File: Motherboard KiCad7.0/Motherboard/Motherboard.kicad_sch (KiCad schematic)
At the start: 49 parts, among them J1 USB_B_Micro, J2 SWD_01x04_Pin, Q1 AO3400A, SW1 SW_STM_RESET, SW2 SW_STM_BOOT_MODE, U1 STM32F103CBT6, U2 AMS1117-3.3, U3 LM66100DCKR, U4 LM66100DCKR, U5 LM66100DCKR, Y1 X322516MMB4SI

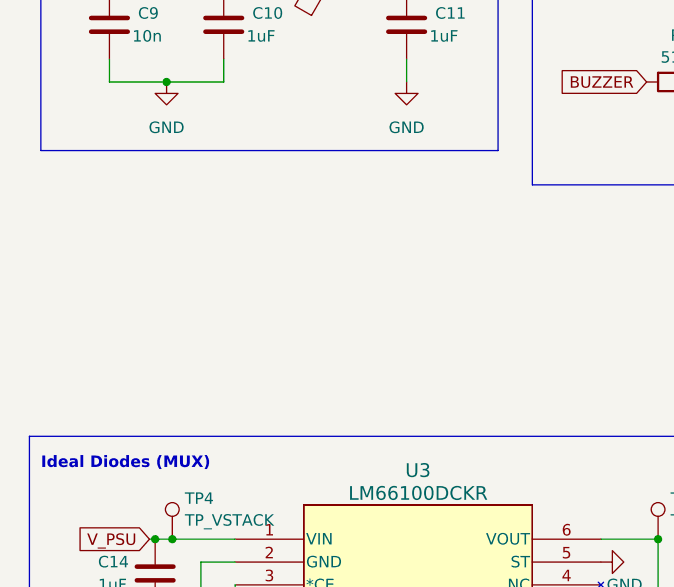
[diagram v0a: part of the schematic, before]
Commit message: Solenoid Valve
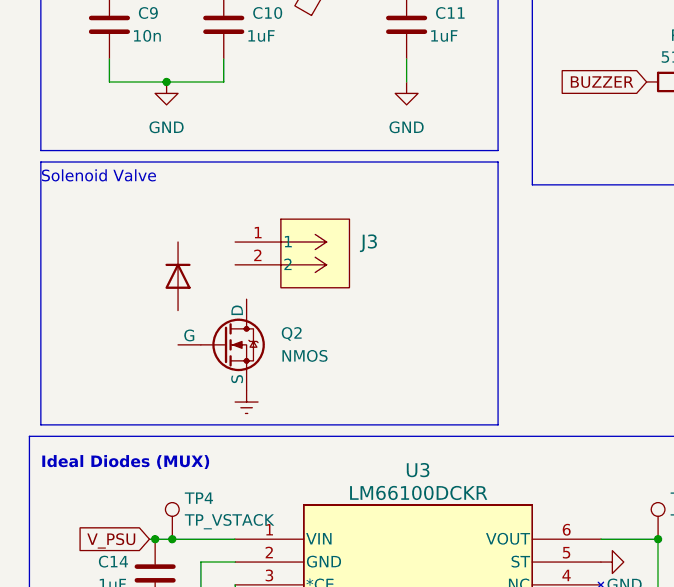
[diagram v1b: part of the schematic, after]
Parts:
- added D6: D, symbol Device:D
- added J3: 2-1445057-2, CONN_2-1445057-2_TYCO, symbol CONN_2-1445057-2_TYCO:2-1445057-2
- added Q2: NMOS, symbol Simulation_SPICE:NMOS
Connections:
- new net Earth: Q2.3 (S)
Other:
- note added: "Solenoid Valve"
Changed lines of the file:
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@@
+    (fill (type none))
+  )
+  (rectangle (start 16.51 99.06) (end 67.31 128.27)
+    (stroke (width 0) (type default))
     (fill (type none))
   )
@@
   (text "USB Connection" (at 102.87 156.21 0)
     (effects (font (size 1.27 1.27) (thickness 0.254) bold) (justify left bottom))
+  )
+  (text "Solenoid Valve\n" (at 16.51 101.6 0)
+    (effects (font (size 1.27 1.27)) (justify left bottom))
   )
   (text "STM32 Decoupling Capacitors for VBAT and VDD" (at 62.23 18.415 0)
@@
     )
   )
+  (symbol (lib_id "power:Earth") (at 39.37 124.46 0) (unit 1)
+    (in_bom yes) (on_board yes) (dnp no) (fields_autoplaced)
+    (property "Reference" "#PWR033" (at 39.37 130.81 0)
+      (effects (font (size 1.27 1.27)) hide)
+    )
+    (property "Value" "Earth" (at 39.37 128.27 0)
+      (effects (font (size 1.27 1.27)) hide)
+    )
+    (property "Footprint" "" (at 39.37 124.46 0)
+      (effects (font (size 1.27 1.27)) hide)
+    )
+    (property "Datasheet" "~" (at 39.37 124.46 0)
+      (effects (font (size 1.27 1.27)) hide)
+    )
+    (pin "1")
+    (instances
+      (project "Motherboard"
+        (path "/6c6aab7b-9fc7-4161-8073-41667e18c629"
+          (reference "#PWR033") (unit 1)
+        )
+      )
+    )
+  )
   (symbol (lib_id "Device:R") (at 91.44 95.25 180) (unit 1)
     (in_bom yes) (on_board yes) (dnp no) (fields_autoplaced)
@@
     )
   )
+  (symbol (lib_id "CONN_2-1445057-2_TYCO:2-1445057-2") (at 38.1 107.95 0) (unit 1)
+    (in_bom yes) (on_board yes) (dnp no) (fields_autoplaced)
+    (property "Reference" "J3" (at 52.07 107.95 0)
+      (effects (font (size 1.524 1.524)) (justify left))
+    )
+    (property "Value" "2-1445057-2" (at 52.07 110.49 0)
+      (effects (font (size 1.524 1.524)) (justify left) hide)
+    )
+    (property "Footprint" "CONN_2-1445057-2_TYCO" (at 38.1 104.14 0)
+      (effects (font (size 1.27 1.27) italic) hide)
+    )
+    (property "Datasheet" "2-1445057-2" (at 38.1 104.14 0)
+      (effects (font (size 1.27 1.27) italic) hide)
+    )
+    (pin "1")
+    (pin "2")
+    (instances
+      (project "Motherboard"
+        (path "/6c6aab7b-9fc7-4161-8073-41667e18c629"
+          (reference "J3") (unit 1)
+        )
+      )
+    )
+  )
   (symbol (lib_id "Device:C") (at 248.92 92.71 0) (unit 1)
     (in_bom yes) (on_board yes) (dnp no)
@@
         (path "/6c6aab7b-9fc7-4161-8073-41667e18c629"
           (reference "C2") (unit 1)
+        )
+      )
+    )
+  )
+  (symbol (lib_id "Device:D") (at 31.75 111.76 270) (unit 1)
+    (in_bom yes) (on_board yes) (dnp no) (fields_autoplaced)
+    (property "Reference" "D6" (at 34.29 110.49 90)
+      (effects (font (size 1.27 1.27)) (justify left) hide)
+    )
+    (property "Value" "D" (at 34.29 113.03 90)
+      (effects (font (size 1.27 1.27)) (justify left) hide)
+    )
+    (property "Footprint" "" (at 31.75 111.76 0)
+      (effects (font (size 1.27 1.27)) hide)
+    )
+    (property "Datasheet" "~" (at 31.75 111.76 0)
+      (effects (font (size 1.27 1.27)) hide)
+    )
+    (property "Sim.Device" "D" (at 31.75 111.76 0)
+      (effects (font (size 1.27 1.27)) hide)
+    )
+    (property "Sim.Pins" "1=K 2=A" (at 31.75 111.76 0)
+      (effects (font (size 1.27 1.27)) hide)
+    )
+    (pin "2")
+    (pin "1")
+    (instances
+      (project "Motherboard"
+        (path "/6c6aab7b-9fc7-4161-8073-41667e18c629"
+          (reference "D6") (unit 1)
         )
       )
@@
         )
       )
+    )
+  )
+  (symbol (lib_id "Simulation_SPICE:NMOS") (at 36.83 119.38 0) (unit 1)
+    (in_bom yes) (on_board yes) (dnp no) (fields_autoplaced)
+    (property "Reference" "Q2" (at 43.18 118.11 0)
+      (effects (font (size 1.27 1.27)) (justify left))
+    )
+    (property "Value" "NMOS" (at 43.18 120.65 0)
+      (effects (font (size 1.27 1.27)) (justify left))
+    )
+    (property "Footprint" "" (at 41.91 116.84 0)
+      (effects (font (size 1.27 1.27)) hide)
+    )
+    (property "Datasheet" "https://ngspice.sourceforge.io/docs/ngspice-manual.pdf" (at 36.83 132.08 0)
+      (effects (font (size 1.27 1.27)) hide)
+    )
+    (property "Sim.Device" "NMOS" (at 36.83 136.525 0)
+      (effects (font (size 1.27 1.27)) hide)
+    )
+    (property "Sim.Type" "VDMOS" (at 36.83 138.43 0)
+      (effects (font (size 1.27 1.27)) hide)
+    )
+    (property "Sim.Pins" "1=D 2=G 3=S" (at 36.83 134.62 0)
+      (effects (font (size 1.27 1.27)) hide)
+    )
+    (pin "1")
+    (pin "2")
+    (pin "3")
+    (instances
+      (project "Motherboard"
+        (path "/6c6aab7b-9fc7-4161-8073-41667e18c629"
+          (reference "Q2") (unit 1)
+        )
+      )

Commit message: Solenoid valve
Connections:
- net +12V: now reaches J3.1
- net +12V: now also D6.1 (K)
- net at J3.2: now also D6.2 (A), Q2.1 (D)
- net +15V: now reaches Q2.2 (G)
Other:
- moved on the sheet: Q2
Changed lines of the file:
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@@
   (junction (at 175.26 110.49) (diameter 0) (color 0 0 0 0)
+  )
+  (junction (at 39.37 114.3) (diameter 0) (color 0 0 0 0)
+  )
+  (junction (at 31.75 107.95) (diameter 0) (color 0 0 0 0)
   )
   (junction (at 29.21 186.69) (diameter 0) (color 0 0 0 0)
@@
     (stroke (width 0) (type default))
   )
+  (wire (pts (xy 25.4 106.68) (xy 25.4 107.95))
+    (stroke (width 0) (type default))
+  )
   (wire (pts (xy 116.84 175.26) (xy 119.38 175.26))
     (stroke (width 0) (type default))
@@
     (stroke (width 0) (type default))
   )
+  (wire (pts (xy 39.37 114.3) (xy 41.91 114.3))
+    (stroke (width 0) (type default))
+  )
   (wire (pts (xy 241.935 67.31) (xy 245.11 67.31))
     (stroke (width 0) (type default))
@@
     (stroke (width 0) (type default))
   )
+  (wire (pts (xy 39.37 115.57) (xy 39.37 114.3))
+    (stroke (width 0) (type default))
+  )
   (wire (pts (xy 38.1 181.61) (xy 34.29 181.61))
     (stroke (width 0) (type default))
@@
     (stroke (width 0) (type default))
   )
+  (wire (pts (xy 38.1 107.95) (xy 31.75 107.95))
+    (stroke (width 0) (type default))
+  )
   (wire (pts (xy 101.6 36.83) (xy 111.76 36.83))
     (stroke (width 0) (type default))
@@
     (stroke (width 0) (type default))
   )
+  (wire (pts (xy 31.75 115.57) (xy 39.37 115.57))
+    (stroke (width 0) (type default))
+  )
   (wire (pts (xy 57.15 87.63) (xy 57.15 90.17))
     (stroke (width 0) (type default))
@@
     (stroke (width 0) (type default))
   )
+  (wire (pts (xy 38.1 114.3) (xy 39.37 114.3))
+    (stroke (width 0) (type default))
+  )
   (wire (pts (xy 260.35 88.9) (xy 264.16 88.9))
     (stroke (width 0) (type default))
@@
     (stroke (width 0) (type default))
   )
+  (wire (pts (xy 38.1 110.49) (xy 38.1 114.3))
+    (stroke (width 0) (type default))
+  )
   (wire (pts (xy 91.44 90.17) (xy 91.44 91.44))
     (stroke (width 0) (type default))
@@
   )
   (wire (pts (xy 175.26 29.21) (xy 172.72 29.21))
+    (stroke (width 0) (type default))
+  )
+  (wire (pts (xy 31.75 107.95) (xy 25.4 107.95))
     (stroke (width 0) (type default))
   )
@@
     )
   )
-  (symbol (lib_id "power:Earth") (at 39.37 124.46 0) (unit 1)
-    (in_bom yes) (on_board yes) (dnp no) (fields_autoplaced)
-    (property "Reference" "#PWR033" (at 39.37 130.81 0)
-      (effects (font (size 1.27 1.27)) hide)
-    )
-    (property "Value" "Earth" (at 39.37 128.27 0)
-      (effects (font (size 1.27 1.27)) hide)
-    )
-    (property "Footprint" "" (at 39.37 124.46 0)
-      (effects (font (size 1.27 1.27)) hide)
-    )
-    (property "Datasheet" "~" (at 39.37 124.46 0)
+  (symbol (lib_id "power:Earth") (at 41.91 124.46 0) (unit 1)
+    (in_bom yes) (on_board yes) (dnp no) (fields_autoplaced)
+    (property "Reference" "#PWR033" (at 41.91 130.81 0)
+      (effects (font (size 1.27 1.27)) hide)
+    )
+    (property "Value" "Earth" (at 41.91 128.27 0)
+      (effects (font (size 1.27 1.27)) hide)
+    )
+    (property "Footprint" "" (at 41.91 124.46 0)
+      (effects (font (size 1.27 1.27)) hide)
+    )
+    (property "Datasheet" "~" (at 41.91 124.46 0)
       (effects (font (size 1.27 1.27)) hide)
     )
@@
     )
   )
+  (symbol (lib_id "power:+12V") (at 25.4 106.68 0) (unit 1)
+    (in_bom yes) (on_board yes) (dnp no)
+    (property "Reference" "#PWR034" (at 25.4 110.49 0)
+      (effects (font (size 1.27 1.27)) hide)
+    )
+    (property "Value" "+12V" (at 25.4 102.87 0)
+      (effects (font (size 1.27 1.27)))
+    )
+    (property "Footprint" "" (at 25.4 106.68 0)
+      (effects (font (size 1.27 1.27)) hide)
+    )
+    (property "Datasheet" "" (at 25.4 106.68 0)
+      (effects (font (size 1.27 1.27)) hide)
+    )
+    (pin "1")
+    (instances
+      (project "Motherboard"
+        (path "/6c6aab7b-9fc7-4161-8073-41667e18c629"
+          (reference "#PWR034") (unit 1)
+        )
+      )
+    )
+  )
   (symbol (lib_id "Device:R") (at 228.6 134.62 180) (unit 1)
     (in_bom yes) (on_board yes) (dnp no) (fields_autoplaced)
@@
     )
   )
+  (symbol (lib_id "power:+15V") (at 34.29 119.38 90) (unit 1)
+    (in_bom yes) (on_board yes) (dnp no) (fields_autoplaced)
+    (property "Reference" "#PWR035" (at 38.1 119.38 0)
+      (effects (font (size 1.27 1.27)) hide)
+    )
+    (property "Value" "+15V" (at 30.48 119.38 90)
+      (effects (font (size 1.27 1.27)) (justify left))
+    )
+    (property "Footprint" "" (at 34.29 119.38 0)
+      (effects (font (size 1.27 1.27)) hide)
+    )
+    (property "Datasheet" "" (at 34.29 119.38 0)
+      (effects (font (size 1.27 1.27)) hide)
+    )
+    (pin "1")
+    (instances
+      (project "Motherboard"
+        (path "/6c6aab7b-9fc7-4161-8073-41667e18c629"
+          (reference "#PWR035") (unit 1)
+        )
+      )
+    )
+  )
   (symbol (lib_id "Device:R") (at 127 179.07 0) (unit 1)
     (in_bom yes) (on_board yes) (dnp no) (fields_autoplaced)
@@
     )
   )
-  (symbol (lib_id "Simulation_SPICE:NMOS") (at 36.83 119.38 0) (unit 1)
-    (in_bom yes) (on_board yes) (dnp no) (fields_autoplaced)
-    (property "Reference" "Q2" (at 43.18 118.11 0)
-      (effects (font (size 1.27 1.27)) (justify left))
-    )
-    (property "Value" "NMOS" (at 43.18 120.65 0)
-      (effects (font (size 1.27 1.27)) (justify left))
-    )
-    (property "Footprint" "" (at 41.91 116.84 0)
-      (effects (font (size 1.27 1.27)) hide)
-    )
-    (property "Datasheet" "https://ngspice.sourceforge.io/docs/ngspice-manual.pdf" (at 36.83 132.08 0)
-      (effects (font (size 1.27 1.27)) hide)
-    )
-    (property "Sim.Device" "NMOS" (at 36.83 136.525 0)
-      (effects (font (size 1.27 1.27)) hide)
-    )
-    (property "Sim.Type" "VDMOS" (at 36.83 138.43 0)
-      (effects (font (size 1.27 1.27)) hide)
-    )
-    (property "Sim.Pins" "1=D 2=G 3=S" (at 36.83 134.62 0)
-      (effects (font (size 1.27 1.27)) hide)
-    )
+  (symbol (lib_id "Simulation_SPICE:NMOS") (at 39.37 119.38 0) (unit 1)
+    (in_bom yes) (on_board yes) (dnp no) (fields_autoplaced)
+    (property "Reference" "Q2" (at 45.72 118.11 0)
+      (effects (font (size 1.27 1.27)) (justify left))
+    )
+    (property "Value" "NMOS" (at 45.72 120.65 0)
+      (effects (font (size 1.27 1.27)) (justify left))
+    )
+    (property "Footprint" "" (at 44.45 116.84 0)
+      (effects (font (size 1.27 1.27)) hide)
+    )
+    (property "Datasheet" "https://ngspice.sourceforge.io/docs/ngspice-manual.pdf" (at 39.37 132.08 0)
+      (effects (font (size 1.27 1.27)) hide)
+    )
+    (property "Sim.Device" "NMOS" (at 39.37 136.525 0)
+      (effects (font (size 1.27 1.27)) hide)
+    )
+    (property "Sim.Type" "VDMOS" (at 39.37 138.43 0)
+      (effects (font (size 1.27 1.27)) hide)
+    )
+    (property "Sim.Pins" "1=D 2=G 3=S" (at 39.37 134.62 0)
+      (effects (font (size 1.27 1.27)) hide)
+    )

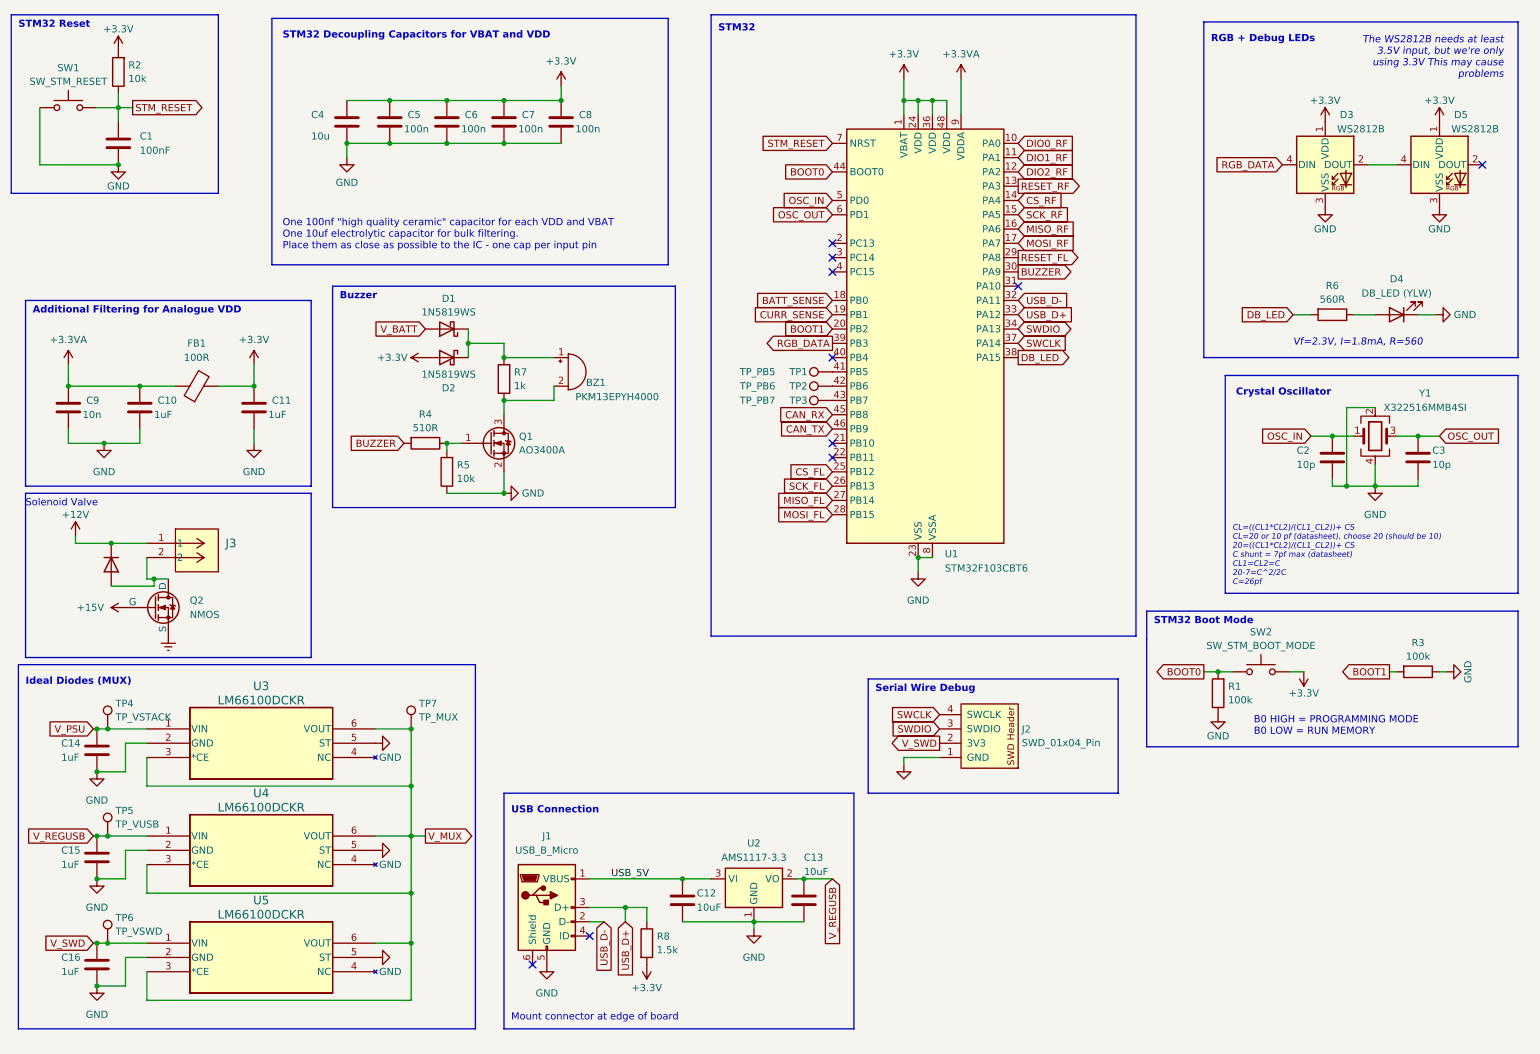
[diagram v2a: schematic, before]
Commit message: Updated solenoid and buzzer circuit
Switched MOSFETs and diodes to use the same as avionics. Moved resistors around in buzzer circuit.
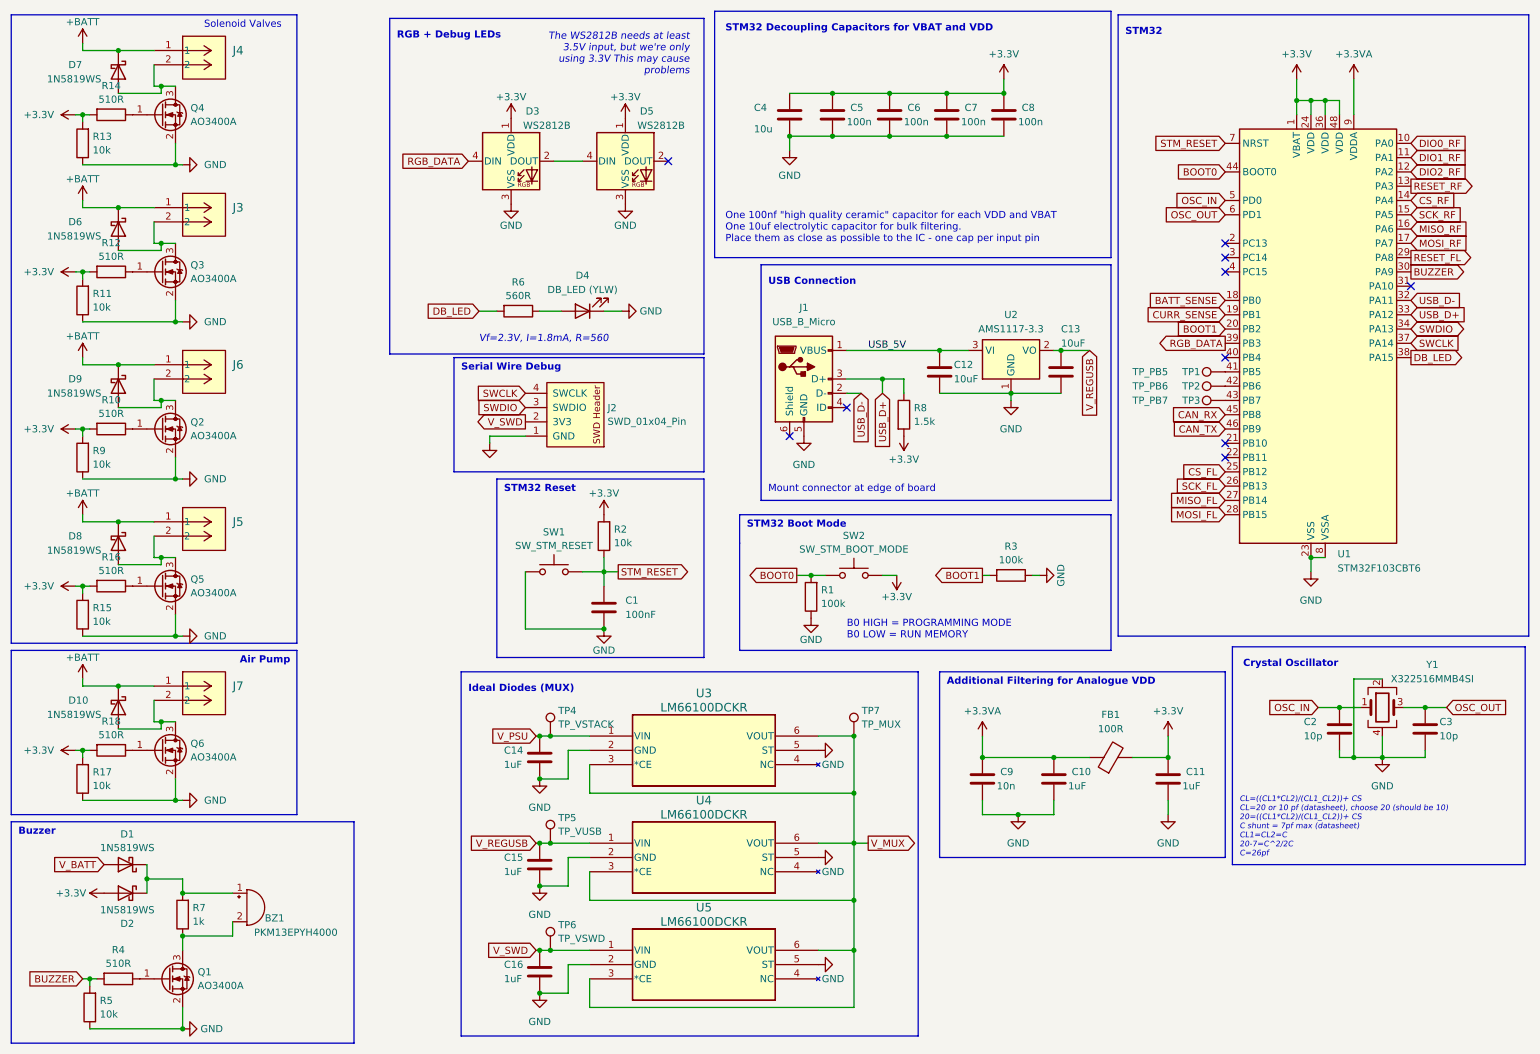
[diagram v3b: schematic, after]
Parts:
- removed D6: D, symbol Device:D
- removed Q2: NMOS, symbol Simulation_SPICE:NMOS
- added D10, D6, D7, D8, D9: 1N5819WS, Diode_SMD:D_SOD-323, symbol Diode:1N5819WS
- added J4, J5, J6, J7: 2-1445057-2, CONN_2-1445057-2_TYCO, symbol CONN_2-1445057-2_TYCO:2-1445057-2
- added Q2, Q3, Q4, Q5, Q6: AO3400A, Package_TO_SOT_SMD:SOT-23, symbol Transistor_FET:AO3400A
- added R10, R12, R14, R16, R18: 510R, Resistor_SMD:R_0603_1608Metric, symbol Device:R
- added R11, R13, R15, R17, R9: 10k, Resistor_SMD:R_0603_1608Metric, symbol Device:R
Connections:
- net +3.3V: now also R10.2, R11.2, R12.2, R13.2, R14.2, R15.2, R16.2, R17.2, R18.2, R9.2
- net BUZZER: now also R5.2
- net GND: now also Q2.2 (S), Q3.2 (S), Q4.2 (S), Q5.2 (S), Q6.2 (S), R11.1, R13.1, R15.1, R17.1, R9.1
- net at Q1.1 (G), R4.1: no longer R5.2
- net at J3.2: now also D6.2 (A), Q3.3 (D)
- net +12V renamed +BATT
- net +BATT: now also D10.1 (K), D6.1 (K), D7.1 (K), D8.1 (K), D9.1 (K), J4.1, J5.1, J6.1, J7.1
- new net: D9.2 (A), J6.2, Q2.3 (D)
- new net: Q5.1 (G), R16.1
- new net: D8.2 (A), J5.2, Q5.3 (D)
- new net: Q4.1 (G), R14.1
- new net: Q3.1 (G), R12.1
- new net: Q6.1 (G), R18.1
- new net: D10.2 (A), J7.2, Q6.3 (D)
- new net: D7.2 (A), J4.2, Q4.3 (D)
- new net: Q2.1 (G), R10.1
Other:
- note added: "Air Pump"
- note added: "Solenoid Valves"
- note removed: "Solenoid Valve"
- moved on the sheet: BZ1, C1, C10, C11, C12, C13, C14, C15, C16, C2, C3, C4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
